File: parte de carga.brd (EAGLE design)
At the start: 100 x 80 mm, 42 parts, among them IC1 MCP73831T-2ACI_OT, IC10 741G3157DBVR, IC15 LMV321AIDCKR, IC16 LMV321AIDCKR, IC2 ESP32-S3-WROOM-1-N16R2, IC3 LMV321AIDCKR, IC5 LMV321AIDCKR, IC7 AD8226ARZ, IC9 LP38692MP-3.3_NOPB, J1 USB3500-30-A-KIT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

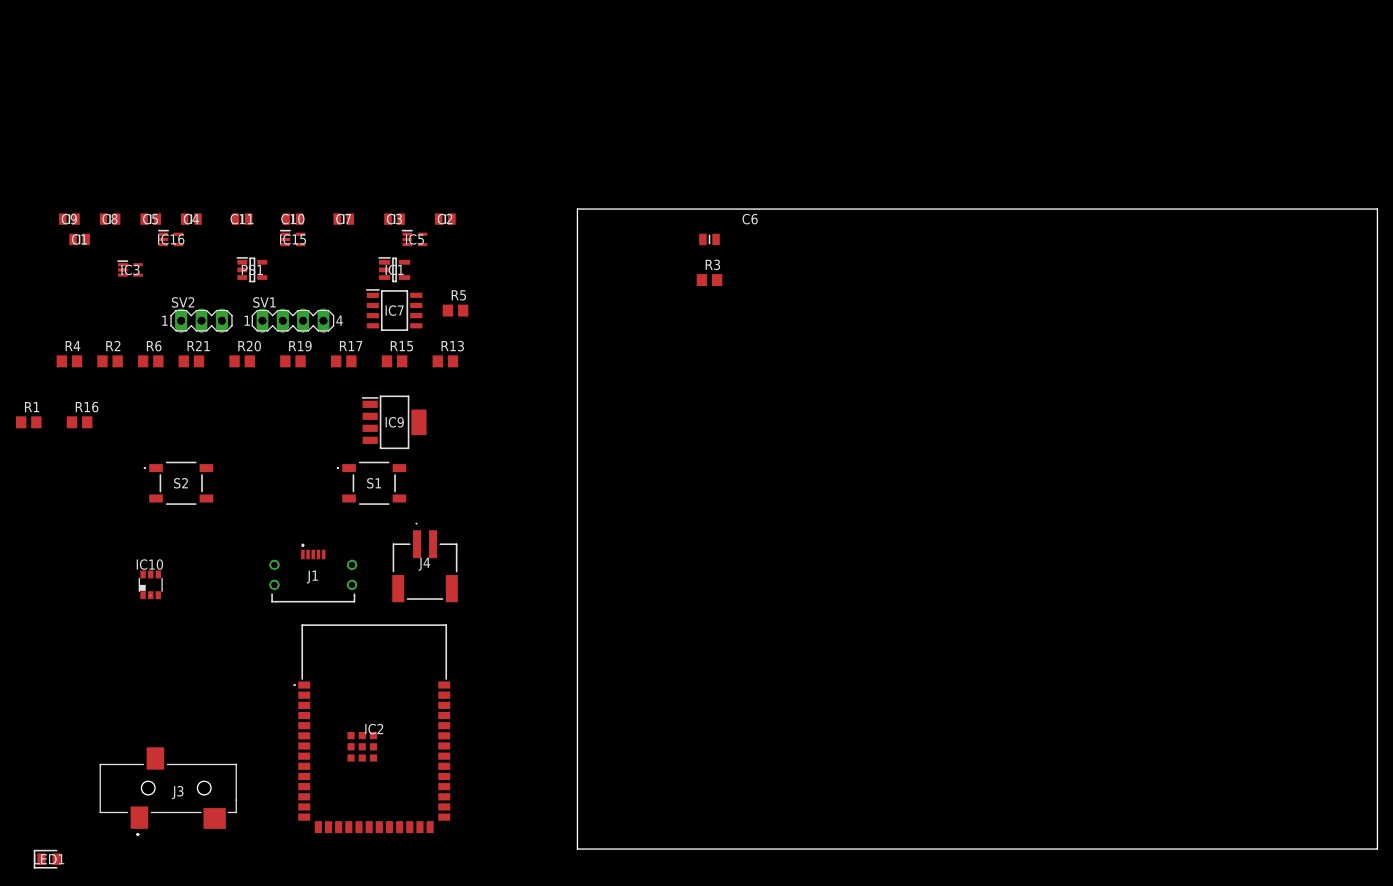
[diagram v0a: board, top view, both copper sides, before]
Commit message: acomode los compenentes dentro de la placa falta organizarlos y elimine una parte de los filtros que no estaba amplificando nada
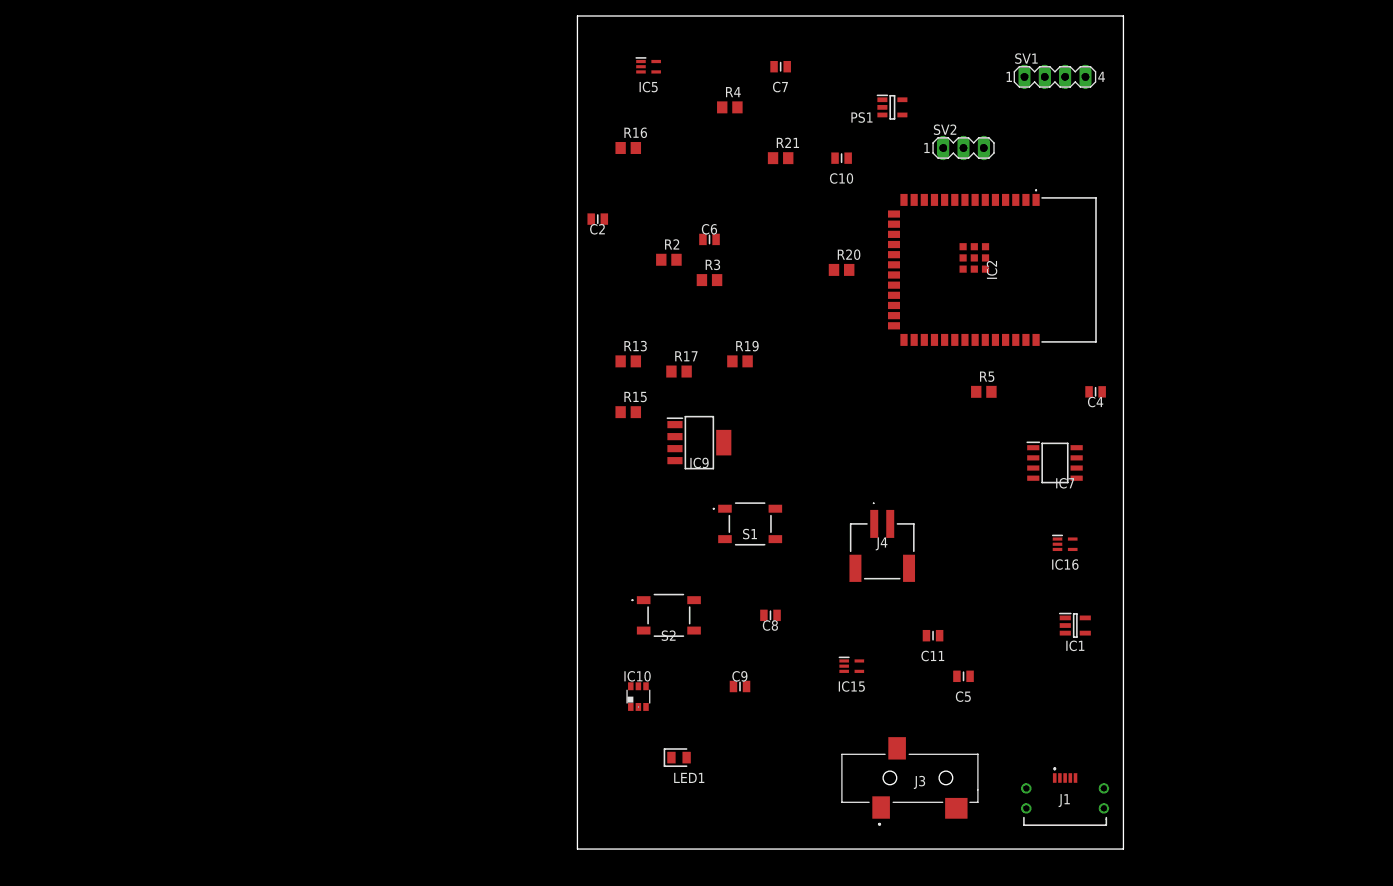
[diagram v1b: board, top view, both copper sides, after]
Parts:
- removed C1: 0.47uF, GCM21B5C2A393JE02L:CAPC2012X140N
- removed C3: 0.1uF, GCM21B5C2A393JE02L:CAPC2012X140N
- removed IC3: LMV321AIDCKR, LMV321AIDCKR:SOT65P210X110-5N
- removed R1: 5.6K, rcl:R0805
- removed R6: 10K, rcl:R0805
- moved IC16 118.1 mm to (61.0, 38.1)
- moved C5 116.6 mm to (48.3, 21.6)
- moved C4 115.1 mm to (64.8, 57.1)
- moved C9 102.2 mm to (20.3, 20.3)
- moved C11 100.8 mm to (44.5, 26.7)
- moved SV1 100.0 mm to (59.7, 96.5)
- moved J1 98.0 mm to (61.0, 5.08)
- moved SV2 97.7 mm to (48.3, 87.6)
- moved IC2 96.3 mm to (52.1, 72.4), turned to 270 degrees
- moved C8 96.3 mm to (24.1, 29.2)
- moved IC1 96.0 mm to (62.2, 27.9)
- moved J3 92.7 mm to (35.6, 8.89)
- moved R4 88.4 mm to (19.1, 92.7)
- moved IC15 87.9 mm to (34.3, 22.9)
- moved IC7 84.7 mm to (59.7, 48.3)
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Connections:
- removed net N$16: C1.1, IC3.3, IC3.4
- removed net N$20: R1.2, R6.1
- removed net N$7: C1.2, C3.2, IC3.1, R6.2
- net +3V3: no longer IC3.5
- net GND: no longer IC3.2
- net N$8: no longer R1.1
- net VOUT1: now also C5.1
- net VSS: no longer C3.1
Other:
- board size 100 x 80 mm -> 68.2 x 104.1 mm
